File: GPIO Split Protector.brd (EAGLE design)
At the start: 75 x 65.1 mm, 31 parts

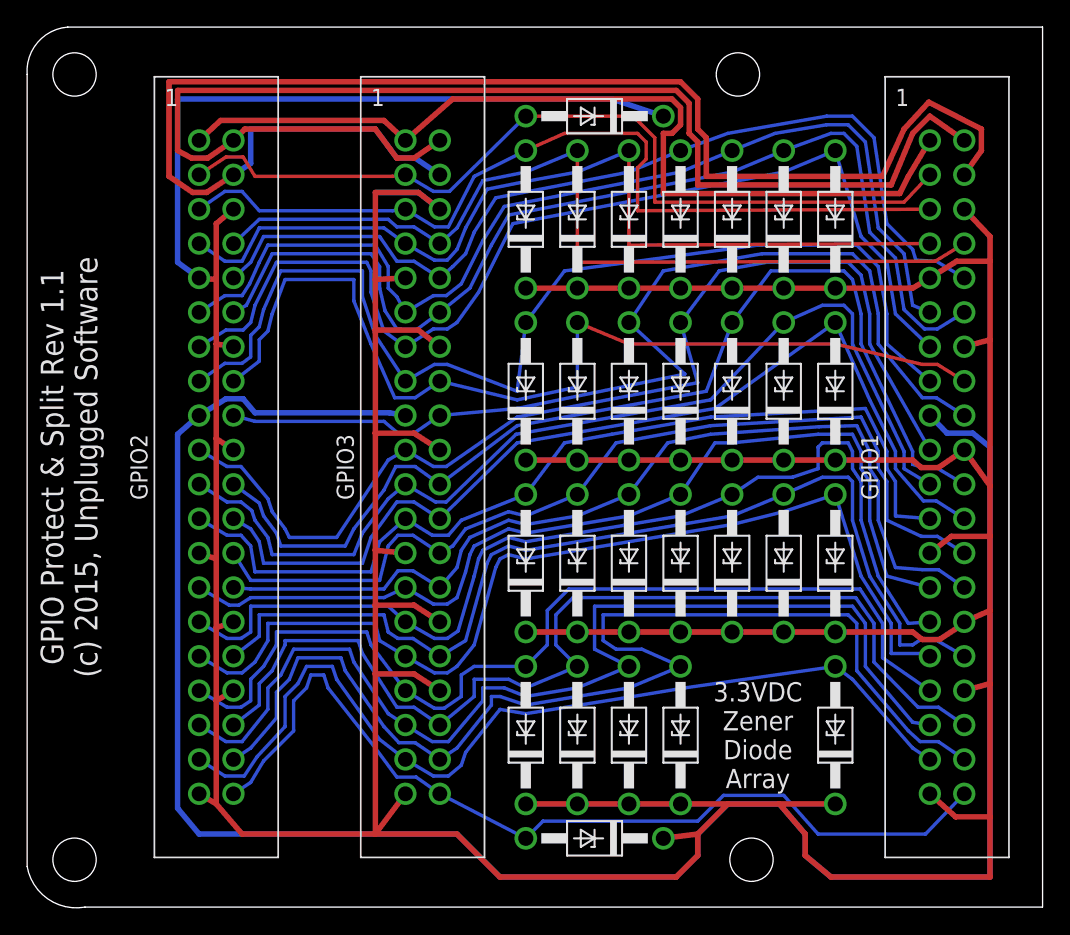
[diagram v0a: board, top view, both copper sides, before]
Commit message: Split TIEVOX Interface into two separate boards, a HAT and a version for the case I will be using that does not satisfy all the HAT requirements.
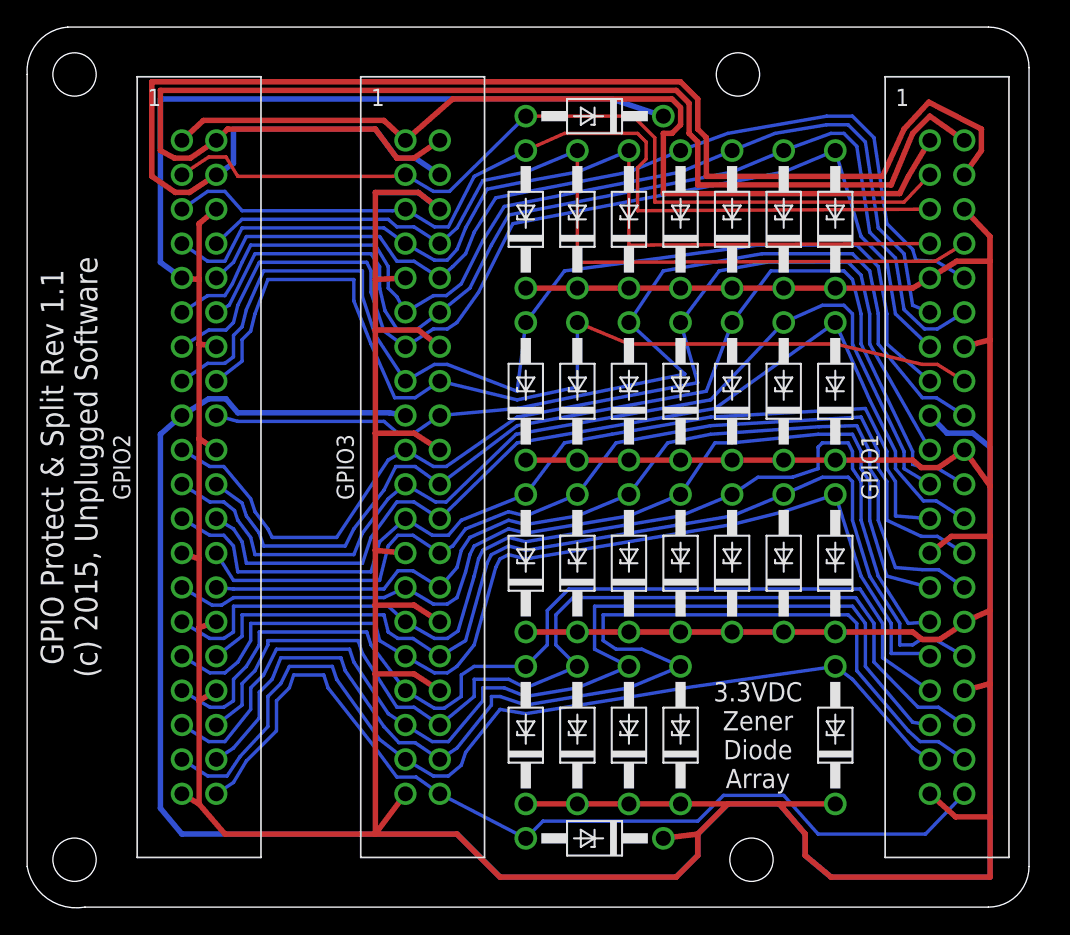
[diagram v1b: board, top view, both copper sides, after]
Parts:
- moved GPIO2 1.27 mm to (12.7, 32.5)
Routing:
- net GND: track 449.0 -> 451.5 mm
- net 3.3VDC2: track 151.5 -> 154.0 mm
- net 5VDC1: track 94.0 -> 96.5 mm
- net 5VDC2: track 105.3 -> 107.8 mm
- net UART_RXD: track 68.8 -> 70.1 mm
- net SPI_SCLK: track 68.2 -> 69.5 mm
- net SPI_MISO: track 73.9 -> 75.1 mm
- net SPI_CE1: track 68.1 -> 69.3 mm
- net GPIO6: track 73.3 -> 74.6 mm
- net GPIO26: track 69.0 -> 70.2 mm
- net GPIO25: track 78.0 -> 79.3 mm
- net GPIO23: track 71.7 -> 72.9 mm
- net GPIO22: track 79.1 -> 80.3 mm
- net GPIO20: track 85.6 -> 86.9 mm
- net GPIO19: track 79.1 -> 80.4 mm
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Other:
- board size 75 x 65.1 mm -> 74 x 65.1 mm
